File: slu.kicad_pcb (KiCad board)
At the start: 2 copper layers, 166 parts, among them sw1 sw_2pos

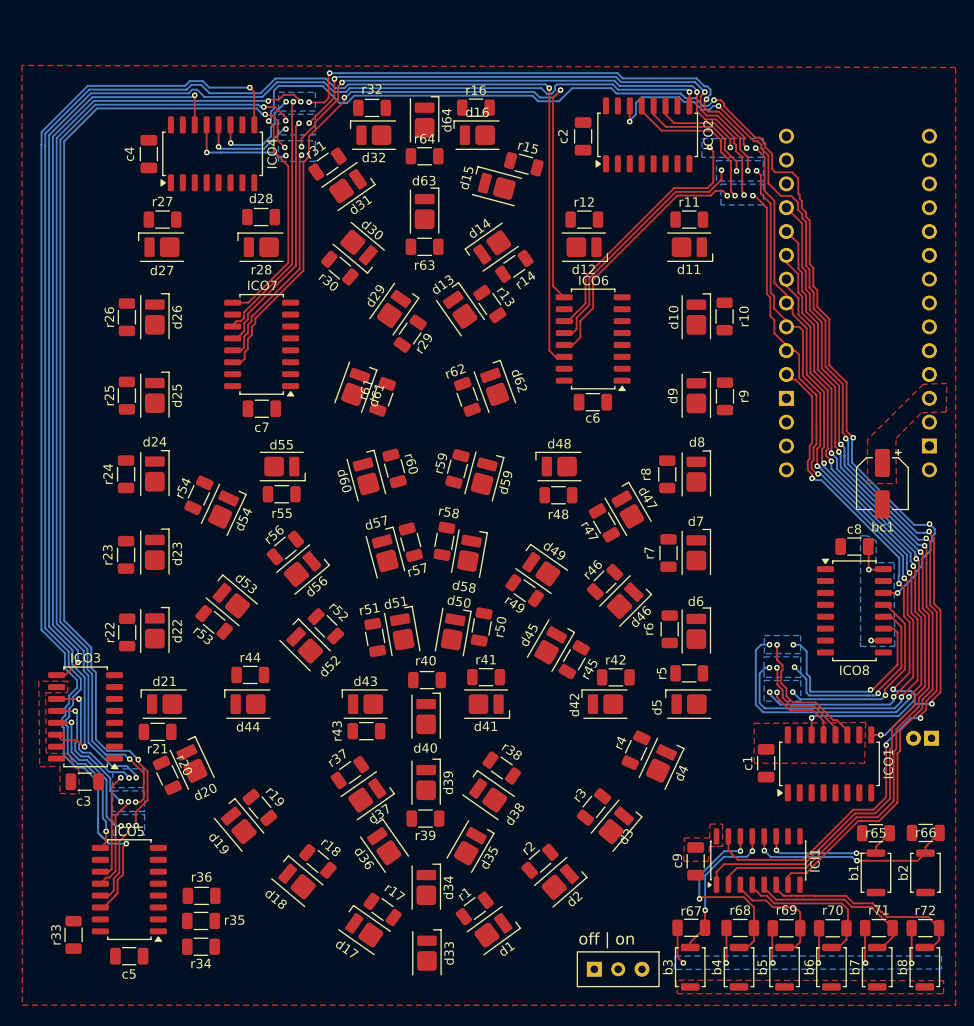
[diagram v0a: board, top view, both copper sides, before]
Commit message: first finished draft all tracks connected
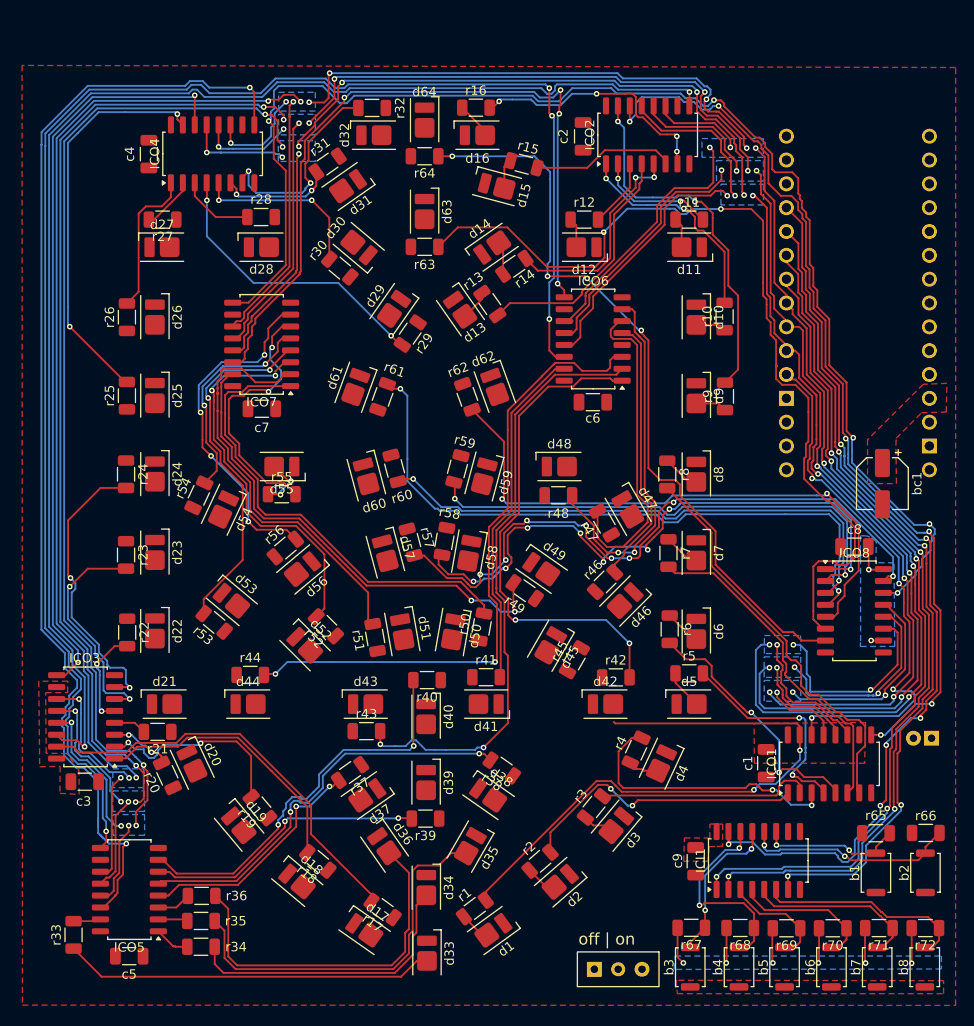
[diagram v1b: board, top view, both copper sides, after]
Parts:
- ICI1: value SOP-16_4.4x10.4mm_P1.27mm -> 74HC165; footprint Package_SO:SO-16_3.9x9.9mm_P1.27mm -> slu_leds_lib:sop16_hc165
- ICO1, ICO2, ICO3, ICO4, ICO5, ICO6, ICO7, ICO8: value SOP-16_4.4x10.4mm_P1.27mm -> 74HC595; footprint Package_SO:SOP-16_4.4x10.4mm_P1.27mm -> slu_leds_lib:sop16_hc595
- b1, b2, b3, b4, b5, b6, b7, b8: value button -> btn; footprint a_detolib:btn_4x3 -> slu_leds_lib:btn_4x3
- bc1: value bulk_cap -> bc10µf_5054; footprint a_detolib:CP_Elec_5x5.4 -> slu_leds_lib:bulkcap_smd
- c1, c2, c3, c4, c5, c6, c7, c8, c9: value c1206 -> 100nf
- d1, d10, d11, d12, d13, d14, d15, d16, d17, d18, d19, d2, d20, d21, d22, d23, d24, d25, d26, d27, d28, d29, d3, d30, d31, d32, d33, d34, d35, d36, d37, d38, d39, d4, d40, d41, d42, d43, d44, d45, d46, d47, d48, d49, d5, d50, d51, d52, d53, d54, d55, d56, d57, d58, d59, d6, d60, d61, d62, d63, d64, d7, d8, d9: value 3528led -> LED; footprint a_detolib:3528led -> slu_leds_lib:blue_led_3528
- r1, r10, r11, r12, r13, r14, r15, r16, r17, r18, r19, r2, r20, r21, r22, r23, r24, r25, r26, r27, r28, r29, r3, r30, r31, r32, r33, r34, r35, r36, r37, r38, r39, r4, r40, r41, r42, r43, r44, r45, r46, r47, r48, r49, r5, r50, r51, r52, r53, r54, r55, r56, r57, r58, r59, r6, r60, r61, r62, r63, r64, r7, r8, r9: value ~ -> 470Ω; footprint a_detolib:r1206 -> slu_leds_lib:r_470Ω_1206
- r65, r66, r67, r68, r69, r70, r71, r72: value ~ -> 10KΩ; footprint a_detolib:r1206 -> slu_leds_lib:r_10KΩ_1206
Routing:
- net /ICD63: track 0.00 -> 96.7 mm, vias 0 -> 2
- net /ICD64: track 0.00 -> 80.5 mm, vias 0 -> 4
- net /ICD57: track 0.00 -> 70.4 mm, vias 0 -> 8
- net /ICD61: track 0.00 -> 70.3 mm, vias 0 -> 2
- net /ICD44: track 0.00 -> 69.0 mm, vias 0 -> 2
- net /ICD58: track 0.00 -> 66.0 mm, vias 0 -> 8
- net /ICD1: track 0.00 -> 64.7 mm, vias 0 -> 2
- net /ICD43: track 0.00 -> 64.6 mm, vias 0 -> 2
- net /ICD62: track 0.00 -> 62.8 mm, vias 0 -> 2
- net /ICD60: track 0.00 -> 58.6 mm, vias 0 -> 2
- net /ICD59: track 0.00 -> 53.8 mm, vias 0 -> 2
- net /ICD42: track 0.00 -> 53.0 mm, vias 0 -> 2
- net /ICD49: track 0.00 -> 52.0 mm, vias 0 -> 2
- net /ICD50: track 0.00 -> 50.1 mm
- net /ICD51: track 0.00 -> 44.7 mm
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
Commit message: most drc flags fixed
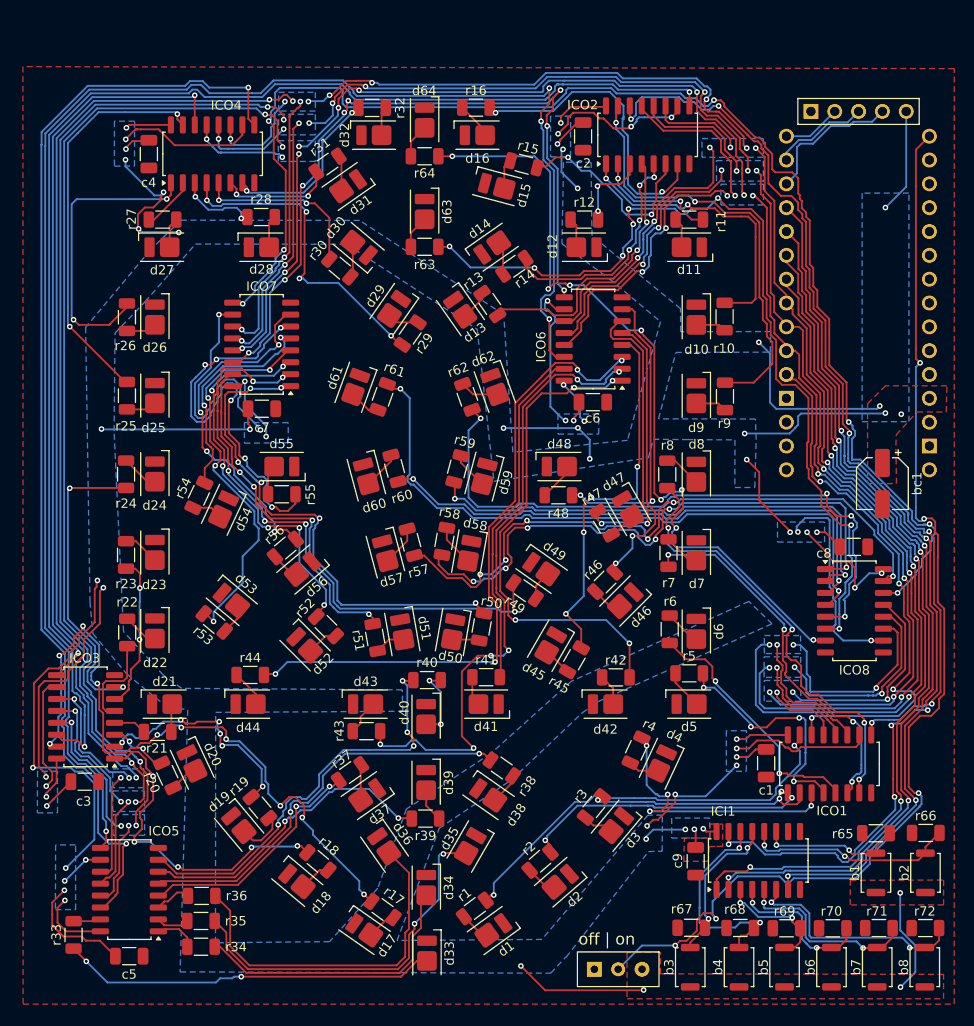
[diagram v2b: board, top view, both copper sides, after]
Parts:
- removed BT1: Battery, a_detolib:btry_18650_foirot
- added J1: lcd_out, a_detolib:5pin_2.54, F.Cu at (146.3, 53.6)
- moved c8 0.07 mm to (145.8, 100.0), turned to 0 degrees
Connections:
- a1 pad 13: unconnected-(a1-D10-Pad13) -> /LCD_LATCH
- a1 pad 14: unconnected-(a1-D11-Pad14) -> /LCD_CLOCK
- a1 pad 15: unconnected-(a1-D12-Pad15) -> /LCD_SERIAL
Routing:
- net +5V: track 5.99 -> 439.8 mm, vias 2 -> 68
- net Net-(a1-D13): track 0.00 -> 121.2 mm, vias 0 -> 5
- net /ICD45: track 0.00 -> 40.6 mm, vias 0 -> 4
- net /ICD17: track 44.3 -> 73.5 mm, vias 0 -> 10
- net GND: track 23.6 -> 0.97 mm, vias 6 -> 0
- net /ICD1: track 64.7 -> 44.8 mm
- net /ICD55: track 28.3 -> 45.0 mm, vias 2 -> 6
- net /ICD26: track 15.8 -> 31.8 mm, vias 0 -> 2
- net /LCD_LATCH: track 0.00 -> 15.1 mm
- net /LCD_CLOCK: track 0.00 -> 10.3 mm
- net /ICD48: track 39.5 -> 31.4 mm
- net Net-(d40-A): track 0.00 -> 7.97 mm, vias 0 -> 2
- net /ICD23: track 24.3 -> 16.5 mm
- net /ICD10: track 23.5 -> 31.3 mm
- net /ICD15: track 15.3 -> 23.0 mm, vias 0 -> 2
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- removed copper zone on B.Cu, net GND
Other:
- board text added: "ICO6"

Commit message: almost done
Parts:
- added BT1: Battery, slu_leds_lib:btry_18650_foirot, B.Cu at (76.4, 98.6)
- added DIO1: SS34, slu_leds_lib:D_SMA, B.Cu at (89.6, 84.8)
- moved sw1 1.29 mm to (120.8, 143.7)
- turned c8 to 180 degrees
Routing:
- net +5V: track 439.8 -> 290.9 mm, vias 68 -> 42
- net /ICD14: track 25.1 -> 41.6 mm, vias 4 -> 7
- net /ICD63: track 96.8 -> 106.0 mm, vias 8 -> 10
- net /SER5-6: track 170.0 -> 179.2 mm, vias 4 -> 6
- net /OE: track 383.7 -> 391.5 mm, vias 29 -> 35
- net /SER6-7: track 80.9 -> 88.4 mm
- net /ICD58: track 63.5 -> 59.8 mm, vias 6 -> 7
- net /ICD41: track 37.0 -> 39.9 mm
- net /ICD13: track 29.8 -> 32.0 mm, vias 2 -> 6
- net /ICD29: track 34.5 -> 36.6 mm
- net /CLOCK: track 389.7 -> 387.6 mm, vias 28 -> 33
- net /SER1-2: track 98.9 -> 96.8 mm
- net /ICD42: track 52.8 -> 54.5 mm
- net /ICD62: track 69.2 -> 67.6 mm, vias 4 -> 6
- net /btn7: track 21.5 -> 20.2 mm
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- added copper zone on B.Cu, net /battery power
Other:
- board text added: "slu fleur de lis | designed by Justin DeKock"

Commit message: recovery, lots of cleanup done
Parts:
- removed BT1: Battery, slu_leds_lib:btry_18650_foirot
- moved c9 0.35 mm to (128.7, 133.8)
- moved c1 0.19 mm to (136.3, 123.1)
- moved c8 0.13 mm to (145.9, 99.9)
- moved d20 0.10 mm to (75.4, 123.2)
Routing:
- net Net-(d36-A): track 38.0 -> 21.7 mm, vias 0 -> 2
- net /ICD23: track 16.5 -> 30.2 mm, vias 2 -> 4
- net /CLOCK: track 387.6 -> 375.2 mm
- net /LATCH: track 384.6 -> 374.0 mm
- net /ICD22: track 10.1 -> 18.9 mm, vias 0 -> 4
- net +5V: track 290.9 -> 298.6 mm, vias 42 -> 50
- net /ICD17: track 73.5 -> 66.7 mm
- net /OE: track 391.5 -> 384.8 mm
- net /SER2-3: track 145.2 -> 139.7 mm
- net /ICD53: track 42.0 -> 36.5 mm
- net Net-(a1-D13): track 119.9 -> 115.9 mm, vias 5 -> 3
- net Net-(d35-A): track 39.5 -> 35.6 mm, vias 2 -> 4
- net /ICD64: track 86.2 -> 89.9 mm
- net /ICD11: track 13.4 -> 17.0 mm
- net /ICD50: track 54.3 -> 50.9 mm, vias 6 -> 4
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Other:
- board outline added: 99.6 x 100.9 mm

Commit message: zero error zero warning recovery
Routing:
- net /ICD14: track 41.9 -> 27.8 mm, vias 7 -> 6
- net /SER5-6: track 178.9 -> 174.4 mm
- net /SER6-7: track 88.4 -> 84.4 mm
- net /ICD29: track 36.6 -> 33.5 mm
- net /ICD63: track 108.9 -> 106.8 mm
- net /CLOCK: track 375.2 -> 373.5 mm
- net +5V: track 298.6 -> 296.9 mm
- net /SER7-8: track 145.0 -> 146.4 mm
- net /LATCH: track 374.0 -> 372.7 mm
- net /ICD64: track 89.9 -> 91.1 mm
- net /ICD54: track 23.8 -> 22.7 mm
- net /ICD28: track 7.86 -> 6.79 mm
- net /ICD15: track 24.2 -> 25.2 mm, vias 2 -> 4

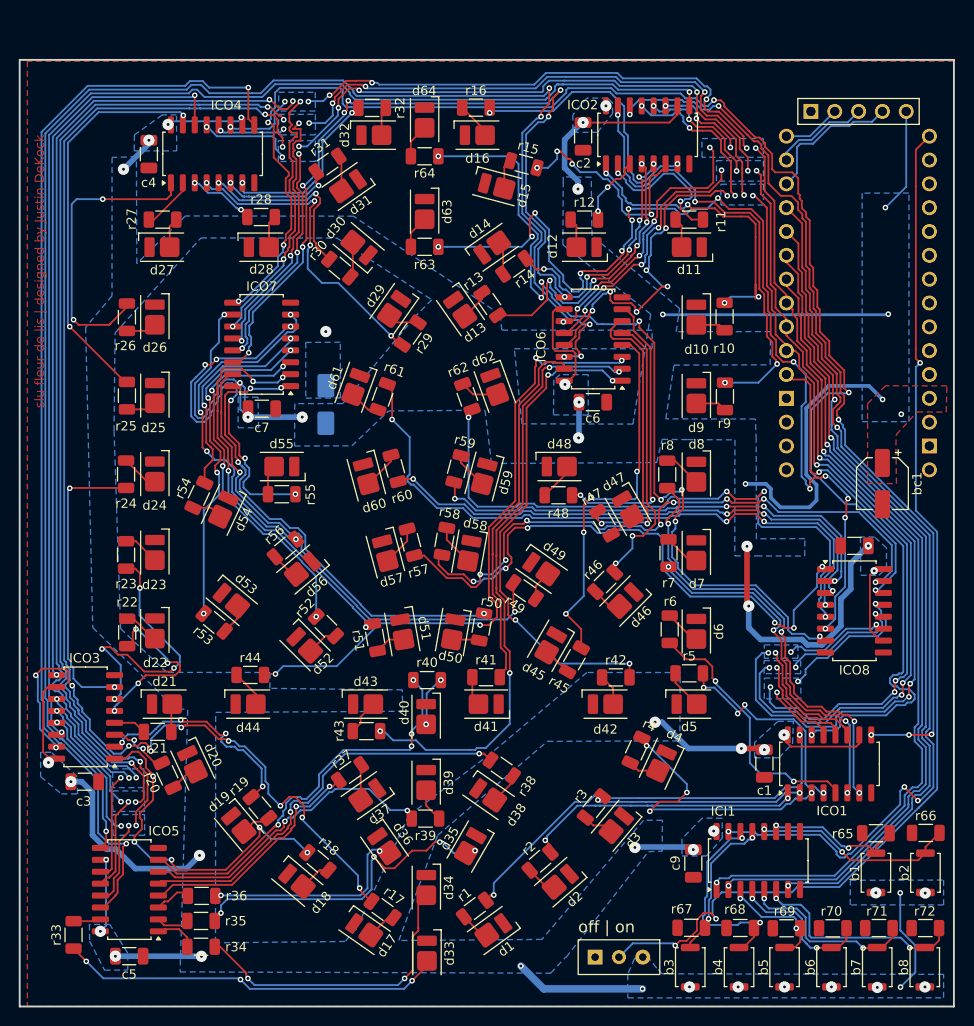
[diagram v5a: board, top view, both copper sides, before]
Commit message: major cleanup of ico7 data traces
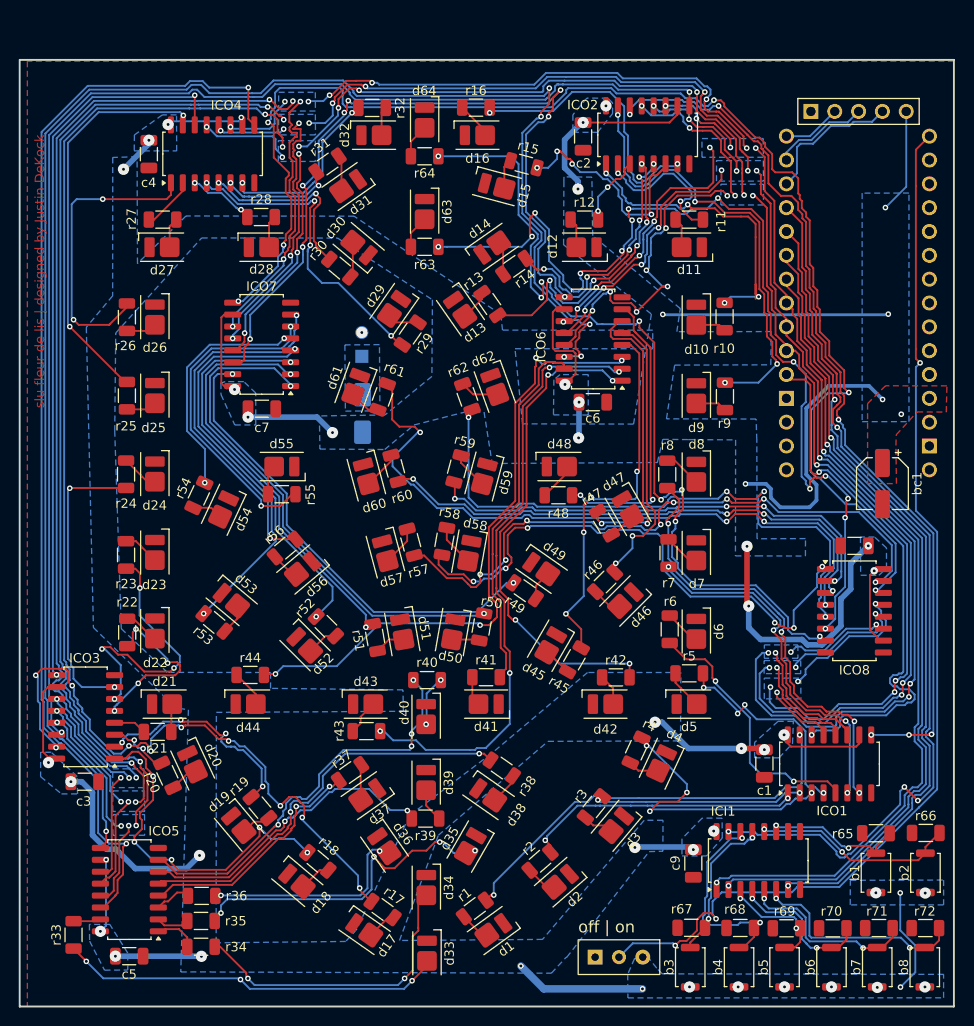
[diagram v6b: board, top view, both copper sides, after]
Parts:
- added BATTERY: Battery, slu_leds_lib:btry_18650_foirot, B.Cu at (80.2, 98.7)
- moved DIODE 4.03 mm to (93.5, 85.8)
- renumbered DIO1 to DIODE
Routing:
- net +5V: track 296.9 -> 281.3 mm, vias 50 -> 49
- net /ICD55: track 43.6 -> 35.2 mm, vias 6 -> 2
- net /ICD53: track 36.7 -> 43.7 mm, vias 4 -> 2
- net /ICD50: track 50.9 -> 54.5 mm, vias 4 -> 2
- net /ICD61: track 68.4 -> 71.7 mm
- net /ICD49: track 54.0 -> 50.6 mm
- net /ICD52: track 39.6 -> 42.4 mm, vias 4 -> 2
- net /ICD54: track 22.7 -> 24.4 mm
- net /ICD56: track 37.8 -> 38.8 mm, vias 4 -> 2
- net /LATCH: track 372.7 -> 371.7 mm
- net /OE: track 385.0 -> 384.5 mm
- net /ICD51: vias 4 -> 2
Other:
- board text added: "+"
- board text added: "-"
- board text added: "ICI1"
- board text added: "ICO1"
- board text added: "ICO2"
- board text added: "ICO3"
- board text added: "ICO4"
- board text added: "ICO5"
- board text added: "ICO7"
- board text added: "ICO8"
